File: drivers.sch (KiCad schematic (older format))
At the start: 120 parts, among them U1 K, U2 E, U3 F, U4 K

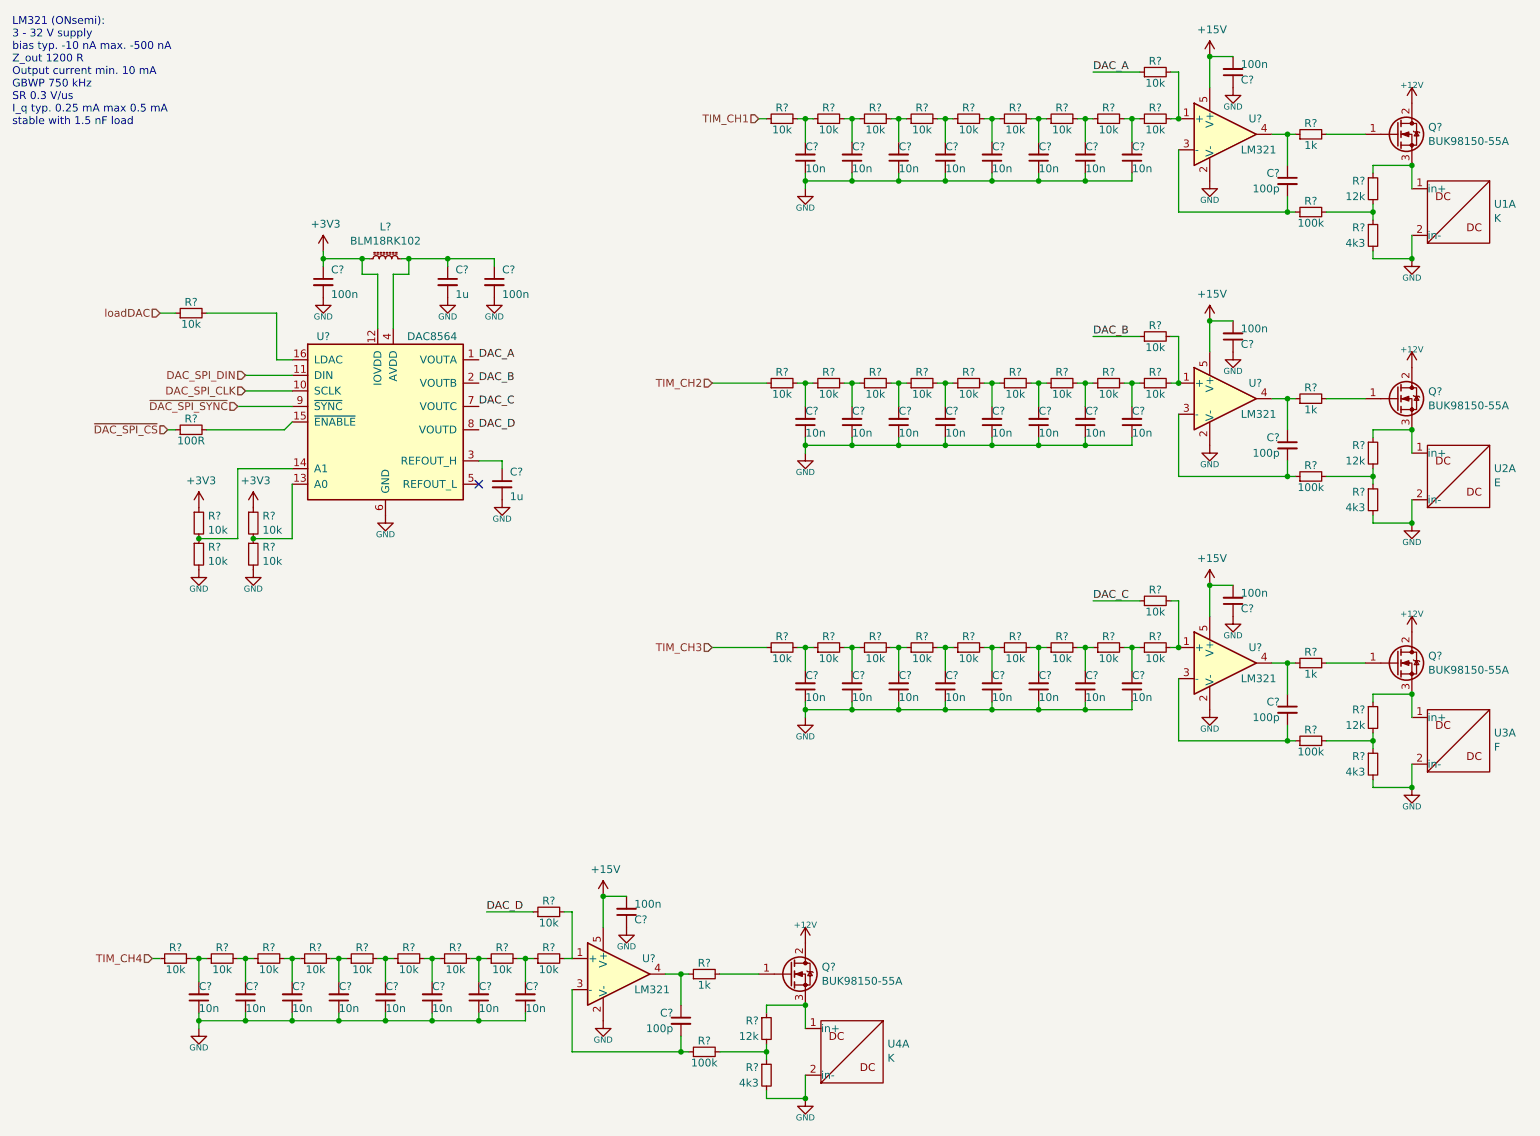
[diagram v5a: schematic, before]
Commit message: - connect things to MCUlow (DAC, screen, keys, debug) - improvement in charger (read PWR key)
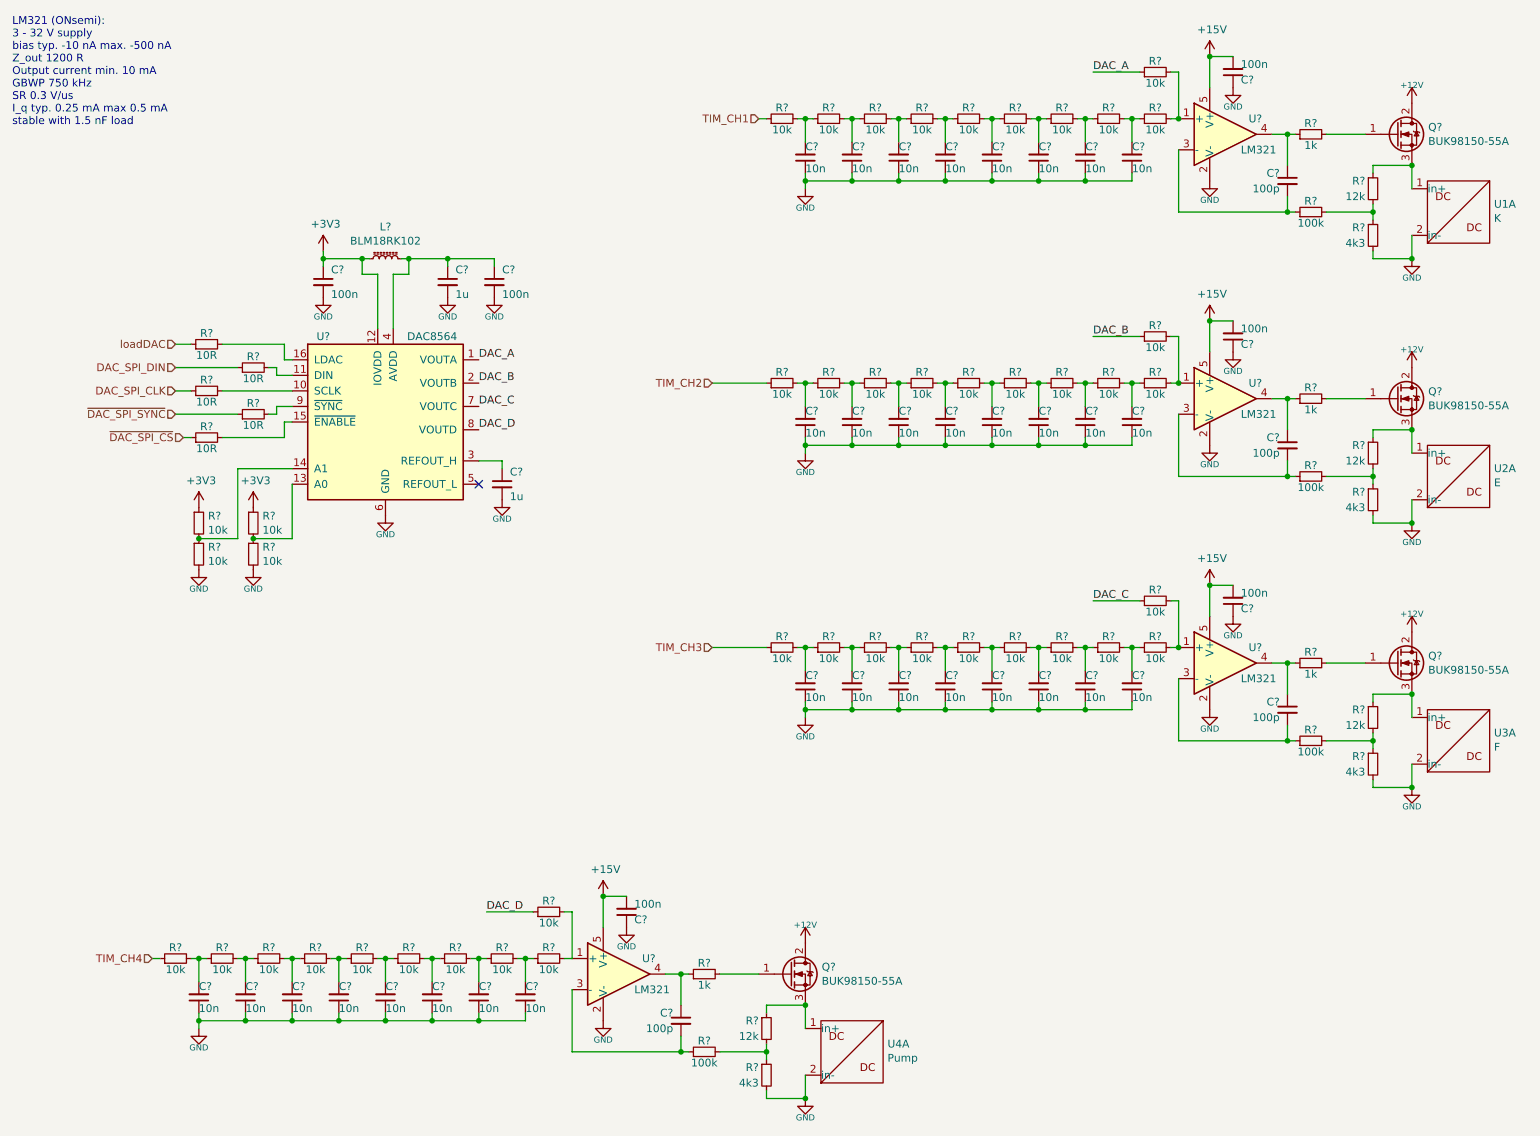
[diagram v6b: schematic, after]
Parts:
- removed R?: 10k, Resistor_SMD:R_0603_1608Metric_Pad1.05x0.95mm_HandSolder, symbol Device:R_Small
- added R? (x4): 10R, Resistor_SMD:R_0603_1608Metric_Pad1.05x0.95mm_HandSolder, symbol Device:R_Small
- L?: footprint (none) -> Resistor_SMD:R_0805_2012Metric_Pad1.15x1.40mm_HandSolder
- R?: value 100R -> 10R
- U4: value K -> Pump
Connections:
- net DAC_SPI_CLK: now also R?.1; no longer U?.10 (SCLK)
- net DAC_SPI_DIN: now also R?.1; no longer U?.11 (DIN)
- net loadDAC: now also R?.1
- net ~DAC_SPI_SYNC: now also R?.1; no longer U?.9 (~SYNC)
- net at U?.16 (LDAC): now also R?.2
- new net: R?.2, U?.11 (DIN)
- new net: R?.2, U?.10 (SCLK)
- new net: R?.2, U?.9 (~SYNC)
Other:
- moved on the sheet: R?
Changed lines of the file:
@@
 AR Path="/5F61C123/5F985527" Ref="U4"  Part="1"
 F 0 "U4" H 6228 7251 50  0000 L CNN
-F 1 "K" H 6228 7160 50  0000 L CNN
+F 1 "Pump" H 6228 7160 50  0000 L CNN
 F 2 "Library_uScope:APD_P2_single" H 6000 7200 50  0001 C CNN
 F 3 "" H 6000 7200 50  0001 C CNN
@@
 AR Path="/5FC7C18C" Ref="#PWR?"  Part="1"
 AR Path="/5F620813/5FC7C18C" Ref="#PWR?"  Part="1"
+AR Path="/5F61C123/5FC7C18C" Ref="#PWR?"  Part="1"
 F 0 "#PWR?" H 3400 2190 50  0001 C CNN
 F 1 "GND" H 3400 2250 39  0000 C TNN
@@
 AR Path="/5FC7C192" Ref="#PWR?"  Part="1"
 AR Path="/5F620813/5FC7C192" Ref="#PWR?"  Part="1"
+AR Path="/5F61C123/5FC7C192" Ref="#PWR?"  Part="1"
 F 0 "#PWR?" H 3700 2190 50  0001 C CNN
 F 1 "GND" H 3700 2250 39  0000 C TNN
@@
 F 0 "L?" V 3205 2100 50  0000 C CNN
 F 1 "BLM18RK102" V 3114 2100 50  0000 C CNN
-F 2 "" H 3000 2100 50  0001 C CNN
+F 2 "Resistor_SMD:R_0805_2012Metric_Pad1.15x1.40mm_HandSolder" H 3000 2100 50  0001 C CNN
 F 3 "~" H 3000 2100 50  0001 C CNN
 	1    3000 2100
@@
 	1    0    0    -1
 $EndComp
-Text HLabel 1550 2450 0    50   Input ~ 0
+Text HLabel 1650 2650 0    50   Input ~ 0
 loadDAC
 $Comp
@@
 $Comp
 L Device:R_Small R?
-U 1 1 600B8FF1
-P 1750 2450
-F 0 "R?" V 1850 2450 50  0000 C BNN
-F 1 "10k" V 1650 2450 50  0000 C TNN
-F 2 "Resistor_SMD:R_0603_1608Metric_Pad1.05x0.95mm_HandSolder" V 1680 2450 50  0001 C CNN
-F 3 "~" H 1750 2450 50  0001 C CNN
-	1    1750 2450
-	0    -1   -1   0
-$EndComp
-$Comp
-L Device:R_Small R?
 U 1 1 600D2659
 P 1650 6600
@@
 $EndComp
 Wire Wire Line
-	1650 2450 1550 2450
-Wire Wire Line
-	2300 2450 2300 2750
-Wire Wire Line
-	2300 2750 2400 2750
-Wire Wire Line
-	1850 2450 2300 2450
+	1750 2650 1650 2650
+Wire Wire Line
+	2350 2750 2400 2750
 Wire Wire Line
 	5750 4600 5700 4600
@@
 	0    -1   -1   0
 $EndComp
-Text HLabel 2100 2850 0    50   Input ~ 0
+Text HLabel 1650 2800 0    50   Input ~ 0
 DAC_SPI_DIN
-Text HLabel 2100 2950 0    50   Input ~ 0
+Text HLabel 1650 2950 0    50   Input ~ 0
 DAC_SPI_CLK
 Wire Wire Line
-	2100 2950 2400 2950
-Wire Wire Line
-	2400 2850 2100 2850
-Text HLabel 1600 3200 0    50   Input ~ 0
+	1650 2950 1750 2950
+Wire Wire Line
+	2050 2800 1650 2800
+Text HLabel 1700 3250 0    50   Input ~ 0
 ~DAC_SPI_CS
 $Comp
 L Device:R_Small R?
 U 1 1 601DDCFB
-P 1750 3200
-F 0 "R?" V 1850 3200 50  0000 C BNN
-F 1 "100R" V 1650 3200 50  0000 C TNN
-F 2 "Resistor_SMD:R_0603_1608Metric_Pad1.05x0.95mm_HandSolder" V 1680 3200 50  0001 C CNN
-F 3 "~" H 1750 3200 50  0001 C CNN
-	1    1750 3200
-	0    -1   -1   0
-$EndComp
-Wire Wire Line
-	1850 3200 2350 3200
-Wire Wire Line
-	2350 3200 2400 3150
-Wire Wire Line
-	1650 3200 1600 3200
-Text HLabel 2050 3050 0    50   Input ~ 0
+P 1850 3250
+F 0 "R?" V 1950 3250 50  0000 C BNN
+F 1 "10R" V 1750 3250 50  0000 C TNN
+F 2 "Resistor_SMD:R_0603_1608Metric_Pad1.05x0.95mm_HandSolder" V 1780 3250 50  0001 C CNN
+F 3 "~" H 1850 3250 50  0001 C CNN
+	1    1850 3250
+	0    -1   -1   0
+$EndComp
+Wire Wire Line
+	2350 3150 2400 3150
+Wire Wire Line
+	1750 3250 1700 3250
+Text HLabel 1650 3100 0    50   Input ~ 0
 ~DAC_SPI_SYNC
 Wire Wire Line
-	2050 3050 2400 3050
+	1650 3100 2050 3100
 $Comp
 L power:GND #PWR?
@@
 AR Path="/602426A8" Ref="#PWR?"  Part="1"
 AR Path="/5F620813/602426A8" Ref="#PWR?"  Part="1"
+AR Path="/5F61C123/602426A8" Ref="#PWR?"  Part="1"
 F 0 "#PWR?" H 3750 3490 50  0001 C CNN
 F 1 "GND" H 3750 3550 39  0000 C TNN
@@
 	3750 3400 3750 3450
 NoConn ~ 3600 3550
+$Comp
+L Device:R_Small R?
+U 1 1 5F9685B2
+P 1850 2650
+F 0 "R?" V 1950 2650 50  0000 C BNN
+F 1 "10R" V 1750 2650 50  0000 C TNN
+F 2 "Resistor_SMD:R_0603_1608Metric_Pad1.05x0.95mm_HandSolder" V 1780 2650 50  0001 C CNN
+F 3 "~" H 1850 2650 50  0001 C CNN
+	1    1850 2650
+	0    -1   -1   0
+$EndComp
+$Comp
+L Device:R_Small R?
+U 1 1 5F98196A
+P 2150 2800
+F 0 "R?" V 2250 2800 50  0000 C BNN
+F 1 "10R" V 2050 2800 50  0000 C TNN
+F 2 "Resistor_SMD:R_0603_1608Metric_Pad1.05x0.95mm_HandSolder" V 2080 2800 50  0001 C CNN
+F 3 "~" H 2150 2800 50  0001 C CNN
+	1    2150 2800
+	0    -1   -1   0
+$EndComp
+$Comp
+L Device:R_Small R?
+U 1 1 5F981A72
+P 1850 2950
+F 0 "R?" V 1950 2950 50  0000 C BNN
+F 1 "10R" V 1750 2950 50  0000 C TNN
+F 2 "Resistor_SMD:R_0603_1608Metric_Pad1.05x0.95mm_HandSolder" V 1780 2950 50  0001 C CNN
+F 3 "~" H 1850 2950 50  0001 C CNN
+	1    1850 2950
+	0    -1   -1   0
+$EndComp
+$Comp
+L Device:R_Small R?
+U 1 1 5F98217A
+P 2150 3100
+F 0 "R?" V 2250 3100 50  0000 C BNN
+F 1 "10R" V 2050 3100 50  0000 C TNN
+F 2 "Resistor_SMD:R_0603_1608Metric_Pad1.05x0.95mm_HandSolder" V 2080 3100 50  0001 C CNN
+F 3 "~" H 2150 3100 50  0001 C CNN
+	1    2150 3100
+	0    -1   -1   0
+$EndComp
+Wire Wire Line
+	2350 2650 2350 2750
+Wire Wire Line
+	2400 2850 2300 2850
+Wire Wire Line
+	2300 2850 2300 2800
+Wire Wire Line
+	2300 2800 2250 2800
+Wire Wire Line
+	2400 3050 2300 3050
+Wire Wire Line
+	2300 3050 2300 3100
+Wire Wire Line
+	2300 3100 2250 3100
+Wire Wire Line
+	2350 3150 2350 3250
+Wire Wire Line
+	2350 3250 1950 3250
+Wire Wire Line
+	2400 2950 1950 2950
+Wire Wire Line
+	2350 2650 1950 2650
 $EndSCHEMATC

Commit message: - final schematic
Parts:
- gave numbers to parts that had none: 119
